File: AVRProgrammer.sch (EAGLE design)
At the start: 58 parts, among them Q1 SI1016CX-T1-GE3SOT-563F, U1 ESDS314, U10 SN74LVC1T45DRL, U11 SN74LVC1T45DRL, U2 XR22404SSOP28, U3 FT230XSSOP16, U4 ATmega88P-20AU A32, U6 CD4572UB, U7 SN74LVC2T45-Q1VSSOP-8, U8 SN74LVC1T45DRL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

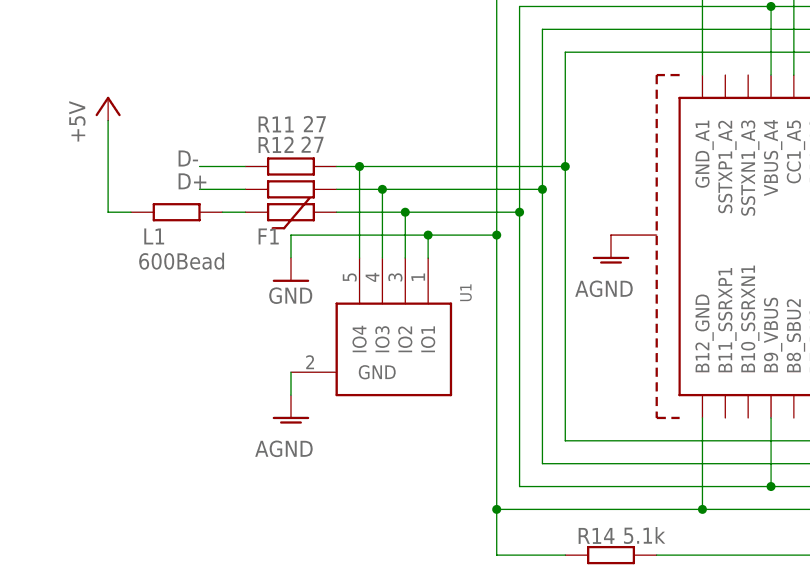
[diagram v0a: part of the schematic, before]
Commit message: Replace incorrect USB ESD component
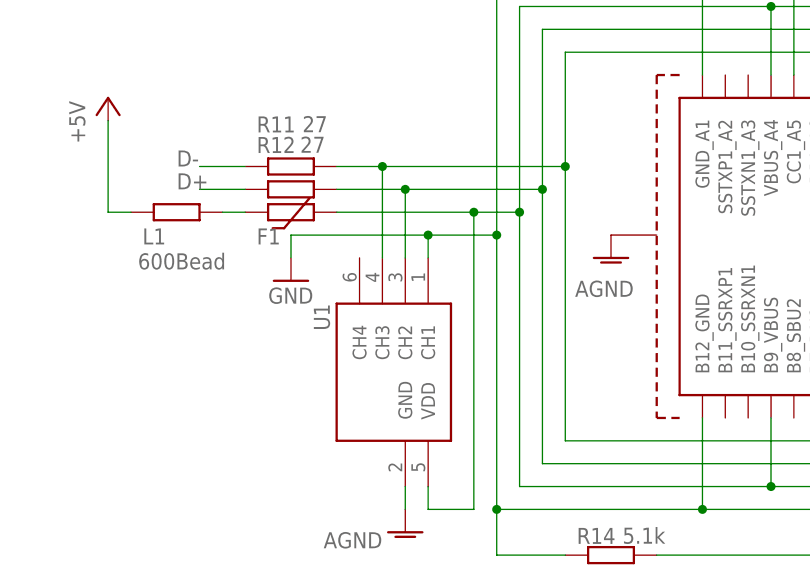
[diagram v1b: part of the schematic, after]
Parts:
- U1: value ESDS314 -> D5V0F4U6SO; device pepin:ESDS314 -> pepin:D5V0F4U6SO
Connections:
- net GND: now also U1.CH1; no longer U1.IO1
- net N$32: now also U1.CH3; no longer U1.IO4
- net N$33: now also U1.CH2; no longer U1.IO3
- net N$34: now also U1.VDD; no longer U1.IO2
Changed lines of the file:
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@@
 <part name="P+10" library="supply1" library_urn="urn:adsk.eagle:library:371" deviceset="+5V" device=""/>
 <part name="F1" library="pepin" deviceset="PTC" device="0805" package3d_urn="urn:adsk.eagle:package:14088533/1" value="MF-PSHT035KX-2"/>
-<part name="U1" library="pepin" deviceset="ESDS314" device="" package3d_urn="urn:adsk.eagle:package:10159336/1"/>
 <part name="AGND2" library="supply1" library_urn="urn:adsk.eagle:library:371" deviceset="AGND" device=""/>
 <part name="GND10" library="supply1" library_urn="urn:adsk.eagle:library:371" deviceset="GND" device=""/>
@@
 <part name="R14" library="rcl" library_urn="urn:adsk.eagle:library:334" deviceset="R-EU_" device="M0805" package3d_urn="urn:adsk.eagle:package:23556/2" value="5.1k"/>
 <part name="R18" library="rcl" library_urn="urn:adsk.eagle:library:334" deviceset="R-EU_" device="M0805" package3d_urn="urn:adsk.eagle:package:23556/2" value="1k"/>
+<part name="U1" library="pepin" deviceset="D5V0F4U6SO" device="" package3d_urn="urn:adsk.eagle:package:11174177/1"/>
 </parts>
 <sheets>
@@
 <attribute name="VALUE" x="382.27" y="55.118" size="1.778" layer="96" display="off"/>
 </instance>
-<instance part="U1" gate="G$1" x="403.86" y="35.56" smashed="yes" rot="R270" grouprefs="IO">
-<attribute name="NAME" x="409.956" y="42.926" size="1.27" layer="95" rot="R270"/>
-</instance>
-<instance part="AGND2" gate="VR1" x="391.16" y="27.94" smashed="yes" grouprefs="IO">
-<attribute name="VALUE" x="393.7" y="25.4" size="1.778" layer="96" rot="R180"/>
+<instance part="AGND2" gate="VR1" x="403.86" y="15.24" smashed="yes" grouprefs="IO">
+<attribute name="VALUE" x="401.32" y="15.24" size="1.778" layer="96" rot="R180"/>
 </instance>
 <instance part="GND10" gate="1" x="388.62" y="78.74" smashed="yes" grouprefs="IO">
@@
 <attribute name="NAME" x="72.39" y="141.1986" size="1.778" layer="95"/>
 <attribute name="VALUE" x="78.74" y="141.224" size="1.778" layer="96"/>
+</instance>
+<instance part="U1" gate="G$1" x="401.32" y="33.02" smashed="yes" rot="R270">
+<attribute name="NAME" x="393.7" y="40.64" size="1.778" layer="95" rot="R270"/>
 </instance>
 </instances>
@@
 <wire x1="414.02" y1="76.2" x2="436.88" y2="76.2" width="0.1524" layer="91" grouprefs="IO"/>
 <junction x="436.88" y="76.2" grouprefs="IO"/>
+<junction x="414.02" y="48.26" grouprefs="IO"/>
 <wire x1="414.02" y1="48.26" x2="406.4" y2="48.26" width="0.1524" layer="91" grouprefs="IO"/>
-<junction x="414.02" y="48.26" grouprefs="IO"/>
-<pinref part="U1" gate="G$1" pin="IO1"/>
+<pinref part="GND7" gate="1" pin="GND"/>
 <wire x1="406.4" y1="48.26" x2="391.16" y2="48.26" width="0.1524" layer="91" grouprefs="IO"/>
-<wire x1="406.4" y1="45.72" x2="406.4" y2="48.26" width="0.1524" layer="91" grouprefs="IO"/>
-<junction x="406.4" y="48.26" grouprefs="IO"/>
-<pinref part="GND7" gate="1" pin="GND"/>
 <wire x1="391.16" y1="45.72" x2="391.16" y2="48.26" width="0.1524" layer="91" grouprefs="IO"/>
 <wire x1="414.02" y1="76.2" x2="414.02" y2="78.74" width="0.1524" layer="91" grouprefs="IO"/>
@@
 <wire x1="414.02" y1="12.7" x2="414.02" y2="17.78" width="0.1524" layer="91" grouprefs="IO"/>
 <junction x="414.02" y="17.78" grouprefs="IO"/>
+<pinref part="U1" gate="G$1" pin="CH1"/>
+<wire x1="406.4" y1="45.72" x2="406.4" y2="48.26" width="0.1524" layer="91"/>
+<junction x="406.4" y="48.26"/>
 </segment>
 <segment>
@@
 <net name="AGND" class="0">
 <segment>
+<pinref part="AGND2" gate="VR1" pin="AGND"/>
+<wire x1="403.86" y1="20.32" x2="403.86" y2="17.78" width="0.1524" layer="91" grouprefs="IO"/>
 <pinref part="U1" gate="G$1" pin="GND"/>
-<pinref part="AGND2" gate="VR1" pin="AGND"/>
-<wire x1="391.16" y1="33.02" x2="391.16" y2="30.48" width="0.1524" layer="91" grouprefs="IO"/>
 </segment>
 <segment>
@@
 <wire x1="452.12" y1="66.04" x2="452.12" y2="68.58" width="0.1524" layer="91" grouprefs="IO"/>
 <wire x1="421.64" y1="68.58" x2="452.12" y2="68.58" width="0.1524" layer="91" grouprefs="IO"/>
-<wire x1="421.64" y1="55.88" x2="398.78" y2="55.88" width="0.1524" layer="91" grouprefs="IO"/>
+<wire x1="421.64" y1="55.88" x2="401.32" y2="55.88" width="0.1524" layer="91" grouprefs="IO"/>
 <junction x="421.64" y="55.88" grouprefs="IO"/>
-<pinref part="U1" gate="G$1" pin="IO4"/>
-<wire x1="398.78" y1="45.72" x2="398.78" y2="55.88" width="0.1524" layer="91" grouprefs="IO"/>
-<junction x="398.78" y="55.88" grouprefs="IO"/>
 <pinref part="R11" gate="G$1" pin="2"/>
-<wire x1="396.24" y1="55.88" x2="398.78" y2="55.88" width="0.1524" layer="91" grouprefs="IO"/>
+<pinref part="U1" gate="G$1" pin="CH3"/>
+<wire x1="401.32" y1="55.88" x2="396.24" y2="55.88" width="0.1524" layer="91" grouprefs="IO"/>
+<wire x1="401.32" y1="45.72" x2="401.32" y2="55.88" width="0.1524" layer="91"/>
+<junction x="401.32" y="55.88"/>
 </segment>
 </net>
@@
 <wire x1="419.1" y1="53.34" x2="419.1" y2="71.12" width="0.1524" layer="91" grouprefs="IO"/>
 <wire x1="419.1" y1="71.12" x2="449.58" y2="71.12" width="0.1524" layer="91" grouprefs="IO"/>
-<wire x1="419.1" y1="53.34" x2="401.32" y2="53.34" width="0.1524" layer="91" grouprefs="IO"/>
+<wire x1="419.1" y1="53.34" x2="403.86" y2="53.34" width="0.1524" layer="91" grouprefs="IO"/>
 <junction x="419.1" y="53.34" grouprefs="IO"/>
-<pinref part="U1" gate="G$1" pin="IO3"/>
-<wire x1="401.32" y1="45.72" x2="401.32" y2="53.34" width="0.1524" layer="91" grouprefs="IO"/>
-<junction x="401.32" y="53.34" grouprefs="IO"/>
 <pinref part="R12" gate="G$1" pin="2"/>
-<wire x1="396.24" y1="53.34" x2="401.32" y2="53.34" width="0.1524" layer="91" grouprefs="IO"/>
+<pinref part="U1" gate="G$1" pin="CH2"/>
+<wire x1="403.86" y1="53.34" x2="396.24" y2="53.34" width="0.1524" layer="91" grouprefs="IO"/>
+<wire x1="403.86" y1="45.72" x2="403.86" y2="53.34" width="0.1524" layer="91"/>
+<junction x="403.86" y="53.34"/>
 </segment>
 </net>
@@
 <wire x1="416.56" y1="73.66" x2="444.5" y2="73.66" width="0.1524" layer="91" grouprefs="IO"/>
 <junction x="444.5" y="73.66" grouprefs="IO"/>
-<wire x1="416.56" y1="50.8" x2="403.86" y2="50.8" width="0.1524" layer="91" grouprefs="IO"/>
+<wire x1="416.56" y1="50.8" x2="411.48" y2="50.8" width="0.1524" layer="91" grouprefs="IO"/>
 <junction x="416.56" y="50.8" grouprefs="IO"/>
-<pinref part="U1" gate="G$1" pin="IO2"/>
-<wire x1="403.86" y1="50.8" x2="396.24" y2="50.8" width="0.1524" layer="91" grouprefs="IO"/>
-<wire x1="403.86" y1="45.72" x2="403.86" y2="50.8" width="0.1524" layer="91" grouprefs="IO"/>
-<junction x="403.86" y="50.8" grouprefs="IO"/>
 <pinref part="F1" gate="G$1" pin="2"/>
-</segment>
-</net>
+<pinref part="U1" gate="G$1" pin="VDD"/>
+<wire x1="411.48" y1="50.8" x2="396.24" y2="50.8" width="0.1524" layer="91" grouprefs="IO"/>
+<wire x1="406.4" y1="20.32" x2="406.4" y2="17.78" width="0.1524" layer="91"/>
+<wire x1="406.4" y1="17.78" x2="411.48" y2="17.78" width="0.1524" layer="91"/>
+<wire x1="411.48" y1="17.78" x2="411.48" y2="50.8" width="0.1524" layer="91"/>
+<junction x="411.48" y="50.8"/>
+</segment>
+</net>
